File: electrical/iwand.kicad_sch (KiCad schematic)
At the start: 13 parts, among them J1 GY-33 (GND DR CT VCC), J2 Speaker 8R, J3 Wake button SW1, J4 LiPo 3.7V (+ -), J5 XIAO BAT+ BAT- link, Q1 AO3400, Q2 AO3400, U1 XIAO ESP32-S3, U3 DFPlayer Mini

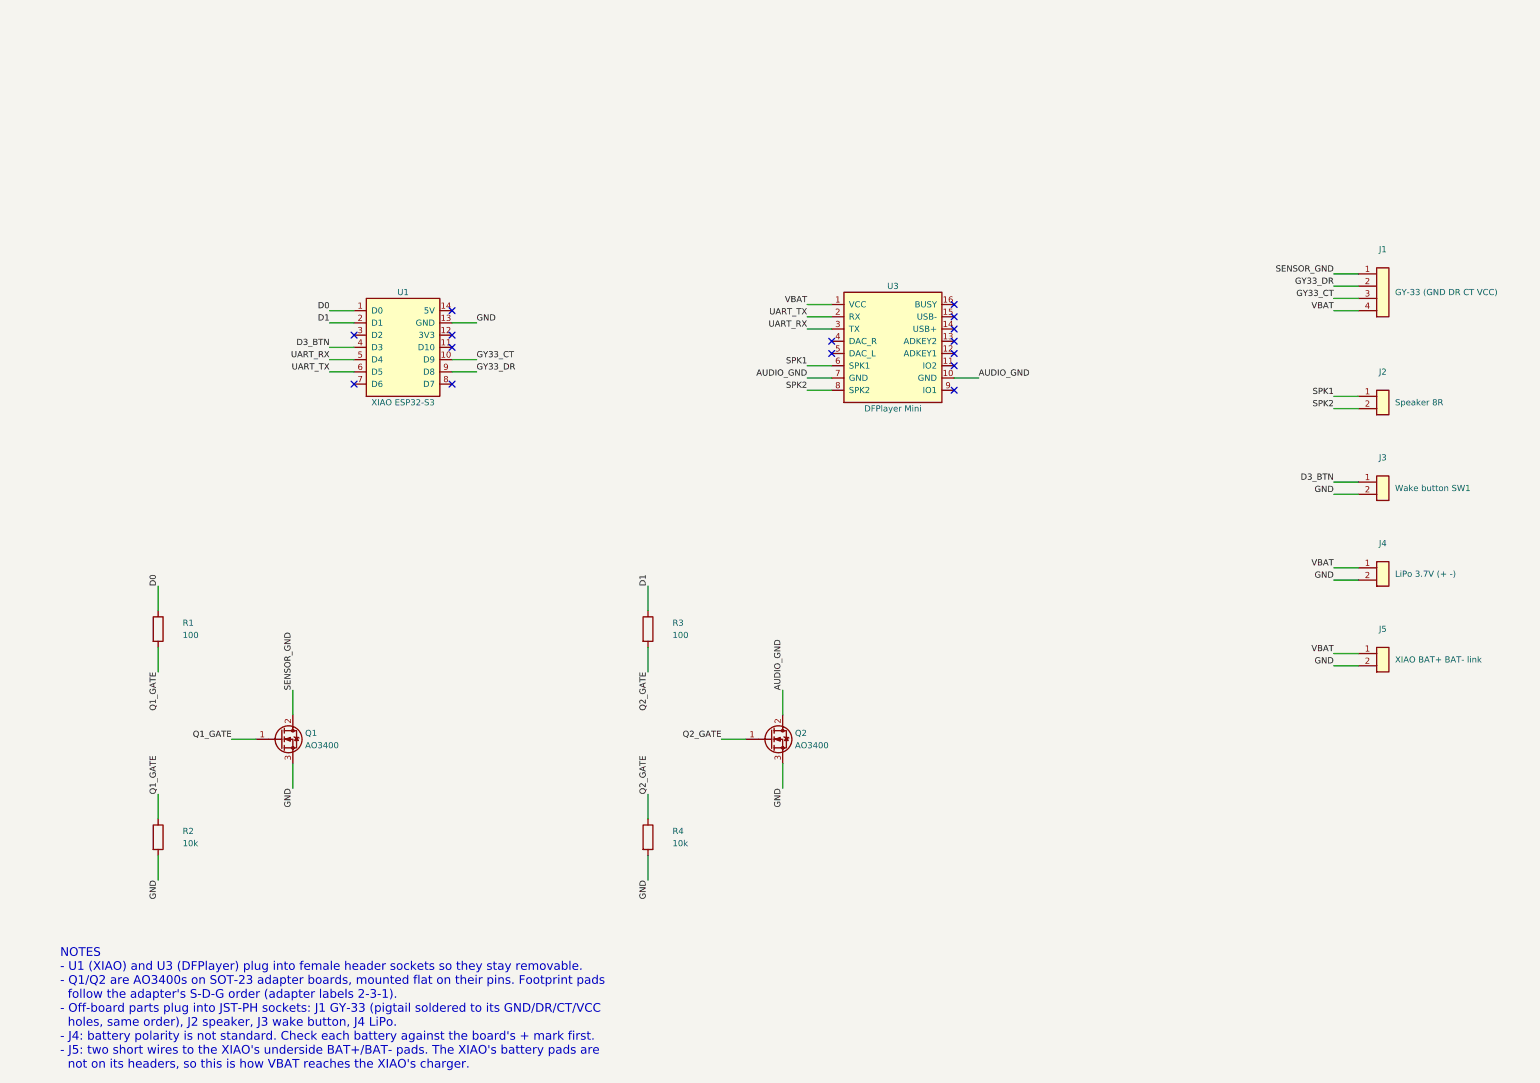
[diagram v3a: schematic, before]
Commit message: Lay out spine PCB; add power switch and battery monitor
- New 75.9 x 22 mm board (iwand.kicad_pcb). Parts run along the wand:
  rear JST plugs (battery, speaker, button), XIAO with USB-C over a long
  edge, MOSFET adapters, DFPlayer, then the GY-33 plug facing forward.
- R1-R6 lie flat under the XIAO. Its courtyard now covers only the
  socket strips and the USB plug, since the module sits ~7.5 mm up in
  low-profile sockets.
- Add SW2, a right-angle slide switch in the battery + lead (J4 -> SW2 ->
  VBAT), so the battery can stay in and charge over the XIAO's USB-C.
  Off disconnects everything, including the charger.
- Add R5/R6 (1M/1M) and C1 (100n) to feed VBAT/2 into D10 (ADC1) for a
  future low-battery warning.
- Show low-profile sockets in 3D using KiCad's socket model scaled to 5 mm.
- Document board size, charging, switch and charge-LED window in the
  electrical, mechanical and firmware notes.

Co-Authored-By: Claude Opus 5.5 <noreply@anthropic.com>
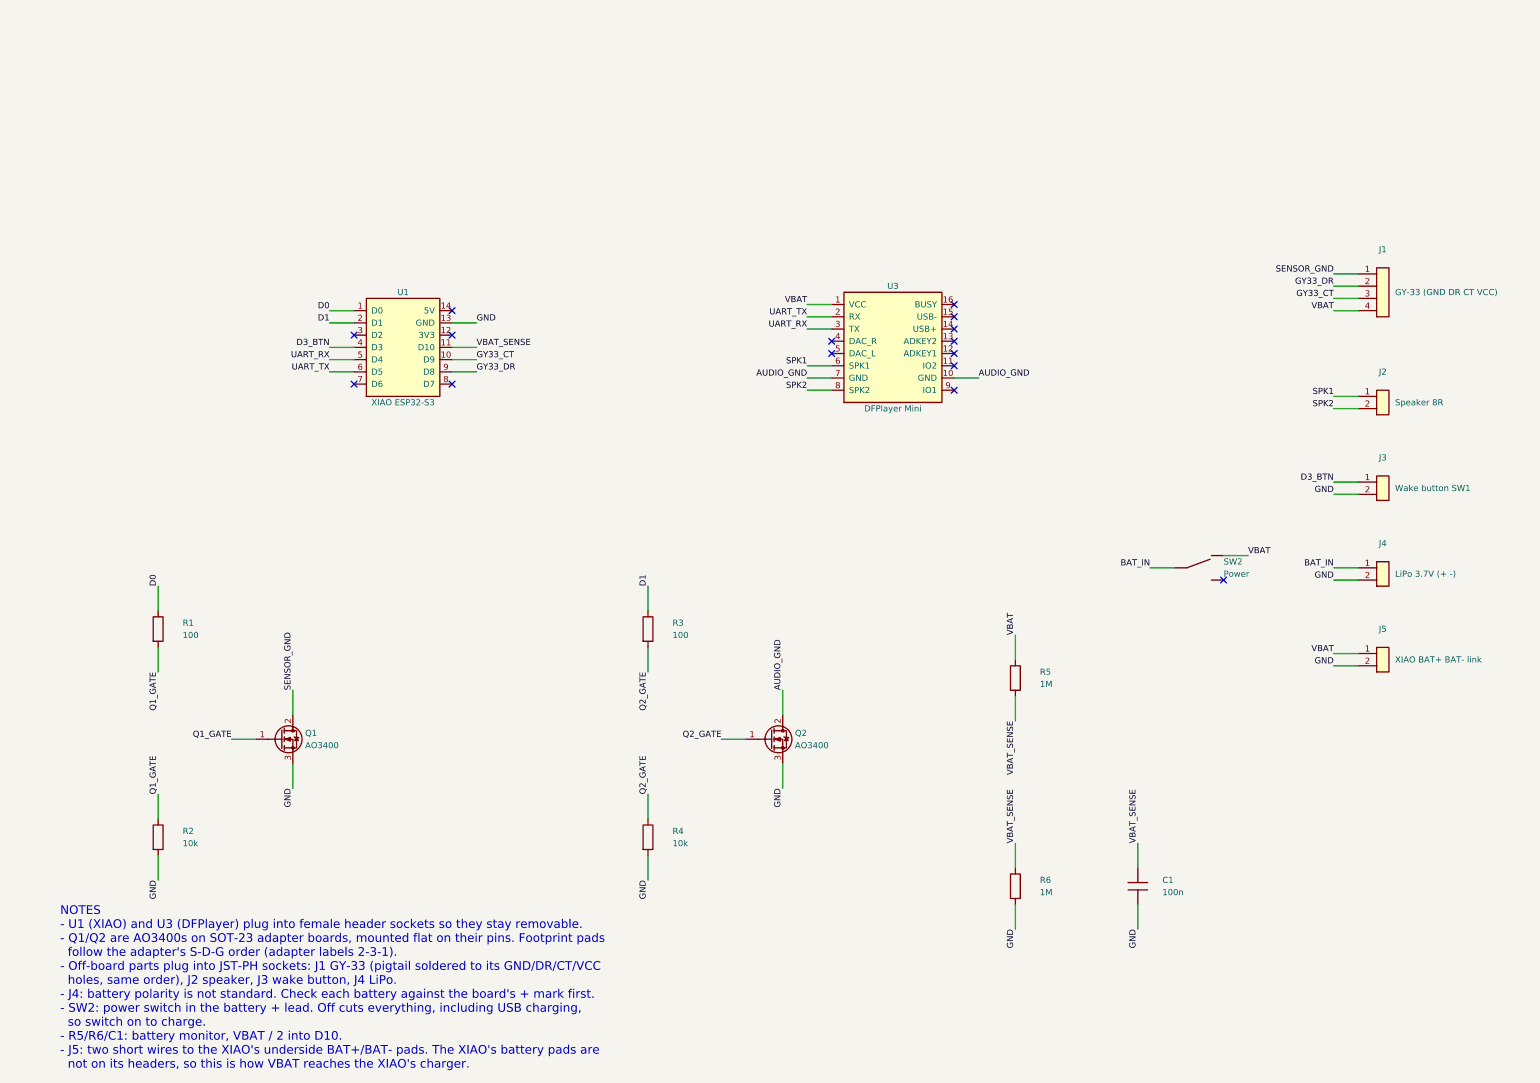
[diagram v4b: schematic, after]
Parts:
- added C1: 100n, Capacitor_THT:C_Disc_D3.0mm_W1.6mm_P2.50mm, symbol Device:C
- added R5, R6: 1M, Resistor_THT:R_Axial_DIN0207_L6.3mm_D2.5mm_P7.62mm_Horizontal, symbol Device:R
- added SW2: Power, Button_Switch_THT:SW_Slide_SPDT_Angled_CK_OS102011MA1Q, symbol Switch:SW_SPDT
- R1, R2, R3, R4: footprint Resistor_THT:R_Axial_DIN0207_L6.3mm_D2.5mm_P2.54mm_Vertical -> Resistor_THT:R_Axial_DIN0207_L6.3mm_D2.5mm_P7.62mm_Horizontal
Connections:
- net GND: now also C1.2, R6.2
- net VBAT: now also R5.1, SW2.1 (A); no longer J4.1 (Pin_1)
- net VBAT_SENSE: now reaches U1.11 (D10)
- net VBAT_SENSE: now also C1.1, R5.2, R6.1
- new net BAT_IN: J4.1 (Pin_1), SW2.2 (B)
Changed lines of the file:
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@@
       (effects (font (size 1.27 1.27)) (justify left))
     )
-    (property "Footprint" "Resistor_THT:R_Axial_DIN0207_L6.3mm_D2.5mm_P2.54mm_Vertical" (at 50.8 147.32 0)
+    (property "Footprint" "Resistor_THT:R_Axial_DIN0207_L6.3mm_D2.5mm_P7.62mm_Horizontal" (at 50.8 147.32 0)
       (effects (font (size 1.27 1.27)) hide)
     )
@@
       (effects (font (size 1.27 1.27)) (justify left))
     )
-    (property "Footprint" "Resistor_THT:R_Axial_DIN0207_L6.3mm_D2.5mm_P2.54mm_Vertical" (at 50.8 190.5 0)
+    (property "Footprint" "Resistor_THT:R_Axial_DIN0207_L6.3mm_D2.5mm_P7.62mm_Horizontal" (at 50.8 190.5 0)
       (effects (font (size 1.27 1.27)) hide)
     )
@@
       (effects (font (size 1.27 1.27)) (justify left))
     )
-    (property "Footprint" "Resistor_THT:R_Axial_DIN0207_L6.3mm_D2.5mm_P2.54mm_Vertical" (at 152.4 147.32 0)
+    (property "Footprint" "Resistor_THT:R_Axial_DIN0207_L6.3mm_D2.5mm_P7.62mm_Horizontal" (at 152.4 147.32 0)
       (effects (font (size 1.27 1.27)) hide)
     )
@@
       (effects (font (size 1.27 1.27)) (justify left))
     )
-    (property "Footprint" "Resistor_THT:R_Axial_DIN0207_L6.3mm_D2.5mm_P2.54mm_Vertical" (at 152.4 190.5 0)
+    (property "Footprint" "Resistor_THT:R_Axial_DIN0207_L6.3mm_D2.5mm_P7.62mm_Horizontal" (at 152.4 190.5 0)
       (effects (font (size 1.27 1.27)) hide)
     )
@@
         (path "/8ff03dcf-b57d-4acb-a5d4-fff50849cfa6"
           (reference "J4") (unit 1)
+        )
+      )
+    )
+  )
+  (symbol (lib_id "Switch:SW_SPDT") (at 266.7 134.62 0) (unit 1)
+    (in_bom yes) (on_board yes) (dnp no)
+    (property "Reference" "SW2" (at 271.78 133.35 0)
+      (effects (font (size 1.27 1.27)) (justify left))
+    )
+    (property "Value" "Power" (at 271.78 135.89 0)
+      (effects (font (size 1.27 1.27)) (justify left))
+    )
+    (property "Footprint" "Button_Switch_THT:SW_Slide_SPDT_Angled_CK_OS102011MA1Q" (at 266.7 134.62 0)
+      (effects (font (size 1.27 1.27)) hide)
+    )
+    (property "Datasheet" "" (at 266.7 134.62 0)
+      (effects (font (size 1.27 1.27)) hide)
+    )
+    (pin "1")
+    (pin "2")
+    (pin "3")
+    (instances
+      (project "iwand"
+        (path "/8ff03dcf-b57d-4acb-a5d4-fff50849cfa6"
+          (reference "SW2") (unit 1)
+        )
+      )
+    )
+  )
+  (symbol (lib_id "Device:R") (at 228.6 157.48 0) (unit 1)
+    (in_bom yes) (on_board yes) (dnp no)
+    (property "Reference" "R5" (at 233.68 156.21 0)
+      (effects (font (size 1.27 1.27)) (justify left))
+    )
+    (property "Value" "1M" (at 233.68 158.75 0)
+      (effects (font (size 1.27 1.27)) (justify left))
+    )
+    (property "Footprint" "Resistor_THT:R_Axial_DIN0207_L6.3mm_D2.5mm_P7.62mm_Horizontal" (at 228.6 157.48 0)
+      (effects (font (size 1.27 1.27)) hide)
+    )
+    (property "Datasheet" "" (at 228.6 157.48 0)
+      (effects (font (size 1.27 1.27)) hide)
+    )
+    (pin "1")
+    (pin "2")
+    (instances
+      (project "iwand"
+        (path "/8ff03dcf-b57d-4acb-a5d4-fff50849cfa6"
+          (reference "R5") (unit 1)
+        )
+      )
+    )
+  )
+  (symbol (lib_id "Device:R") (at 228.6 200.66 0) (unit 1)
+    (in_bom yes) (on_board yes) (dnp no)
+    (property "Reference" "R6" (at 233.68 199.39 0)
+      (effects (font (size 1.27 1.27)) (justify left))
+    )
+    (property "Value" "1M" (at 233.68 201.93 0)
+      (effects (font (size 1.27 1.27)) (justify left))
+    )
+    (property "Footprint" "Resistor_THT:R_Axial_DIN0207_L6.3mm_D2.5mm_P7.62mm_Horizontal" (at 228.6 200.66 0)
+      (effects (font (size 1.27 1.27)) hide)
+    )
+    (property "Datasheet" "" (at 228.6 200.66 0)
+      (effects (font (size 1.27 1.27)) hide)
+    )
+    (pin "1")
+    (pin "2")
+    (instances
+      (project "iwand"
+        (path "/8ff03dcf-b57d-4acb-a5d4-fff50849cfa6"
+          (reference "R6") (unit 1)
+        )
+      )
+    )
+  )
+  (symbol (lib_id "Device:C") (at 254 200.66 0) (unit 1)
+    (in_bom yes) (on_board yes) (dnp no)
+    (property "Reference" "C1" (at 259.08 199.39 0)
+      (effects (font (size 1.27 1.27)) (justify left))
+    )
+    (property "Value" "100n" (at 259.08 201.93 0)
+      (effects (font (size 1.27 1.27)) (justify left))
+    )
+    (property "Footprint" "Capacitor_THT:C_Disc_D3.0mm_W1.6mm_P2.50mm" (at 254 200.66 0)
+      (effects (font (size 1.27 1.27)) hide)
+    )
+    (property "Datasheet" "" (at 254 200.66 0)
+      (effects (font (size 1.27 1.27)) hide)
+    )
+    (pin "1")
+    (pin "2")
+    (instances
+      (project "iwand"
+        (path "/8ff03dcf-b57d-4acb-a5d4-fff50849cfa6"
+          (reference "C1") (unit 1)
         )
       )
@@
     (effects (font (size 1.27 1.27)) (justify left bottom))
   )
-  (no_connect (at 111.76 88.9))
+  (wire (pts (xy 111.76 88.9) (xy 116.84 88.9))
+    (stroke (width 0) (type default))
+  )
+  (label "VBAT_SENSE" (at 116.84 88.9 0)
+    (effects (font (size 1.27 1.27)) (justify left bottom))
+  )
   (no_connect (at 111.76 86.36))
   (wire (pts (xy 111.76 83.82) (xy 116.84 83.82))
@@
     (stroke (width 0) (type default))
   )
-  (label "VBAT" (at 294.64 134.62 180)
+  (label "BAT_IN" (at 294.64 134.62 180)
     (effects (font (size 1.27 1.27)) (justify right bottom))
   )
@@
     (effects (font (size 1.27 1.27)) (justify right bottom))
   )
+  (wire (pts (xy 271.78 132.08) (xy 276.86 132.08))
+    (stroke (width 0) (type default))
+  )
+  (label "VBAT" (at 276.86 132.08 0)
+    (effects (font (size 1.27 1.27)) (justify left bottom))
+  )
+  (wire (pts (xy 261.62 134.62) (xy 256.54 134.62))
+    (stroke (width 0) (type default))
+  )
+  (label "BAT_IN" (at 256.54 134.62 180)
+    (effects (font (size 1.27 1.27)) (justify right bottom))
+  )
+  (no_connect (at 271.78 137.16))
+  (wire (pts (xy 228.6 153.67) (xy 228.6 148.59))
+    (stroke (width 0) (type default))
+  )
+  (label "VBAT" (at 228.6 148.59 90)
+    (effects (font (size 1.27 1.27)) (justify left bottom))
+  )
+  (wire (pts (xy 228.6 161.29) (xy 228.6 166.37))
+    (stroke (width 0) (type default))
+  )
+  (label "VBAT_SENSE" (at 228.6 166.37 270)
+    (effects (font (size 1.27 1.27)) (justify right bottom))
+  )
+  (wire (pts (xy 228.6 196.85) (xy 228.6 191.77))
+    (stroke (width 0) (type default))
+  )
+  (label "VBAT_SENSE" (at 228.6 191.77 90)
+    (effects (font (size 1.27 1.27)) (justify left bottom))
+  )
+  (wire (pts (xy 228.6 204.47) (xy 228.6 209.55))
+    (stroke (width 0) (type default))
+  )
+  (label "GND" (at 228.6 209.55 270)
+    (effects (font (size 1.27 1.27)) (justify right bottom))
+  )
+  (wire (pts (xy 254 196.85) (xy 254 191.77))
+    (stroke (width 0) (type default))
+  )
+  (label "VBAT_SENSE" (at 254 191.77 90)
+    (effects (font (size 1.27 1.27)) (justify left bottom))
+  )
+  (wire (pts (xy 254 204.47) (xy 254 209.55))
+    (stroke (width 0) (type default))
+  )
+  (label "GND" (at 254 209.55 270)
+    (effects (font (size 1.27 1.27)) (justify right bottom))
+  )
   (wire (pts (xy 299.72 152.4) (xy 294.64 152.4))
     (stroke (width 0) (type default))
@@
     (effects (font (size 1.27 1.27)) (justify right bottom))
   )
-  (text "NOTES\n- U1 (XIAO) and U3 (DFPlayer) plug into female header sockets so they stay removable.\n- Q1/Q2 are AO3400s on SOT-23 adapter boards, mounted flat on their pins. Footprint pads\n  follow the adapter's S-D-G order (adapter labels 2-3-1).\n- Off-board parts plug into JST-PH sockets: J1 GY-33 (pigtail soldered to its GND/DR/CT/VCC\n  holes, same order), J2 speaker, J3 wake button, J4 LiPo.\n- J4: battery polarity is not standard. Check each battery against the board's + mark first.\n- J5: two short wires to the XIAO's underside BAT+/BAT- pads. The XIAO's battery pads are\n  not on its headers, so this is how VBAT reaches the XIAO's charger." (at 30.48 238.76 0)
+  (text "NOTES\n- U1 (XIAO) and U3 (DFPlayer) plug into female header sockets so they stay removable.\n- Q1/Q2 are AO3400s on SOT-23 adapter boards, mounted flat on their pins. Footprint pads\n  follow the adapter's S-D-G order (adapter labels 2-3-1).\n- Off-board parts plug into JST-PH sockets: J1 GY-33 (pigtail soldered to its GND/DR/CT/VCC\n  holes, same order), J2 speaker, J3 wake button, J4 LiPo.\n- J4: battery polarity is not standard. Check each battery against the board's + mark first.\n- SW2: power switch in the battery + lead. Off cuts everything, including USB charging,\n  so switch on to charge.\n- R5/R6/C1: battery monitor, VBAT / 2 into D10.\n- J5: two short wires to the XIAO's underside BAT+/BAT- pads. The XIAO's battery pads are\n  not on its headers, so this is how VBAT reaches the XIAO's charger." (at 30.48 238.76 0)
     (effects (font (size 1.8 1.8) (thickness 0.25)) (justify left bottom))
   )

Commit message: Board v0.3: visible J4 polarity marks, JST-PH socket for J5
J4's +/- silkscreen marks sat under the JST housing, so a reversed
battery plug went unnoticed. Move the front marks clear of the housing,
add matching marks on the back beside BAT, and note in the README that
J4 is the reverse of most LiPo plugs.

Replace the J5 pin header (XIAO BAT+/BAT- link) with a JST PH top-entry
socket (B2B-PH-K). It is lower than a header and Dupont plug and takes
the same PHR-2 plug as J1-J4. A side-entry S2B-PH-K doesn't fit between
Q2 and SW2. Re-route the nearby GND and VBAT tracks to the new pads.

Bump the revision to v0.3 and regenerate the Gerbers, drill files and
the populated PCB STEP model.

Co-Authored-By: Claude Opus 5.5 <noreply@anthropic.com>
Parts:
- J5: footprint Connector_PinHeader_2.54mm:PinHeader_1x02_P2.54mm_Vertical -> Connector_JST:JST_PH_B2B-PH-K_1x02_P2.00mm_Vertical
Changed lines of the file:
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@@
     (title "iWand")
     (date "")
-    (rev "v0.2")
+    (rev "v0.3")
     (comment 1 "Sensor+MOSFET power gating, DFPlayer audio, GY-33 UART")
   )
@@
       (effects (font (size 1.27 1.27)) (justify left))
     )
-    (property "Footprint" "Connector_PinHeader_2.54mm:PinHeader_1x02_P2.54mm_Vertical" (at 304.8 152.4 0)
-      (effects (font (size 1.27 1.27)) hide)
-    )
+    (property "Footprint" "Connector_JST:JST_PH_B2B-PH-K_1x02_P2.00mm_Vertical" (at 304.8 152.4 0)
+      (effects (font (size 1.27 1.27)) hide)
+    )
